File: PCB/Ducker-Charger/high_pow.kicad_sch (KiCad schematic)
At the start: 75 parts, among them Q13 BSC040N08NS5, Q15 SI7157DP-T1-GE3, Q3 BSC040N08NS5, Q4 BSC040N08NS5, Q5 BSC040N08NS5, U1 BQ25713RSNR, U2 TPS25750DRJKR

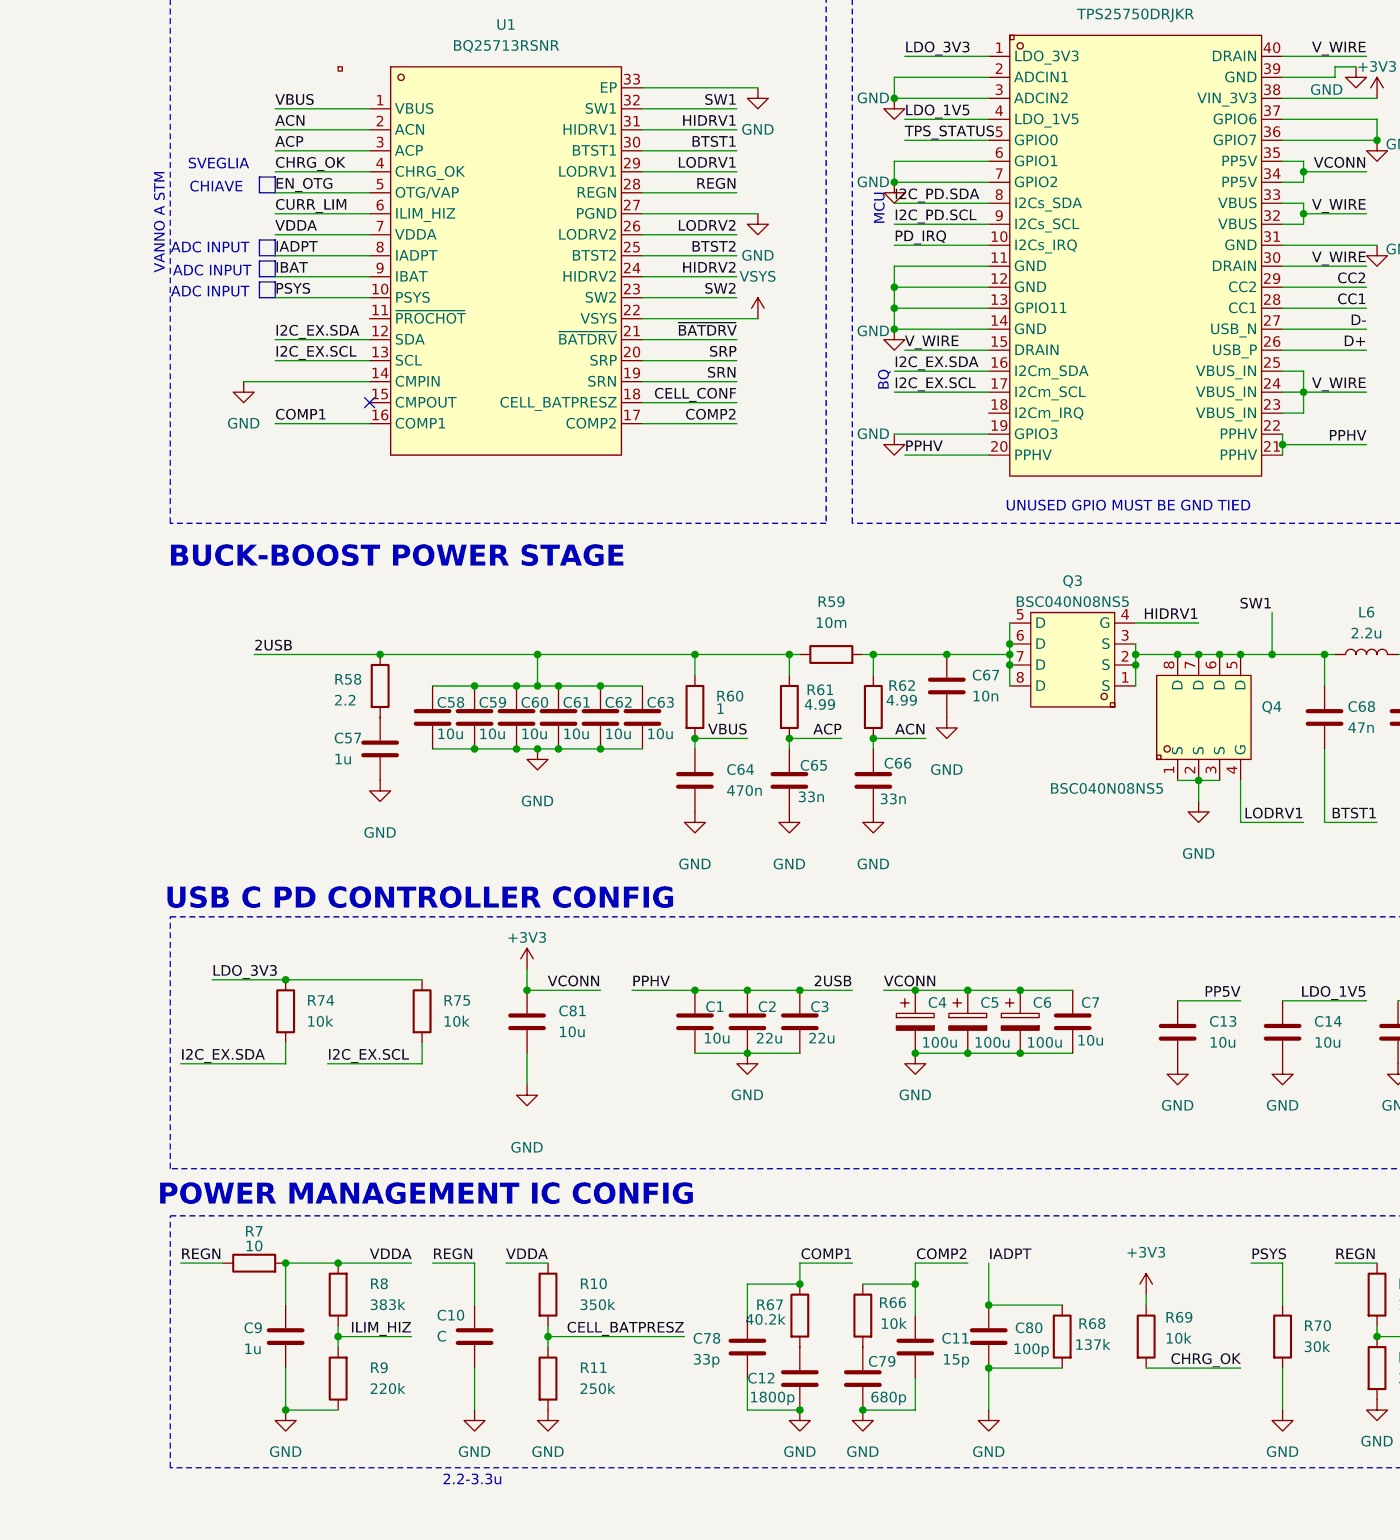
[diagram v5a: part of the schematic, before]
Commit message: fix: MCU connections
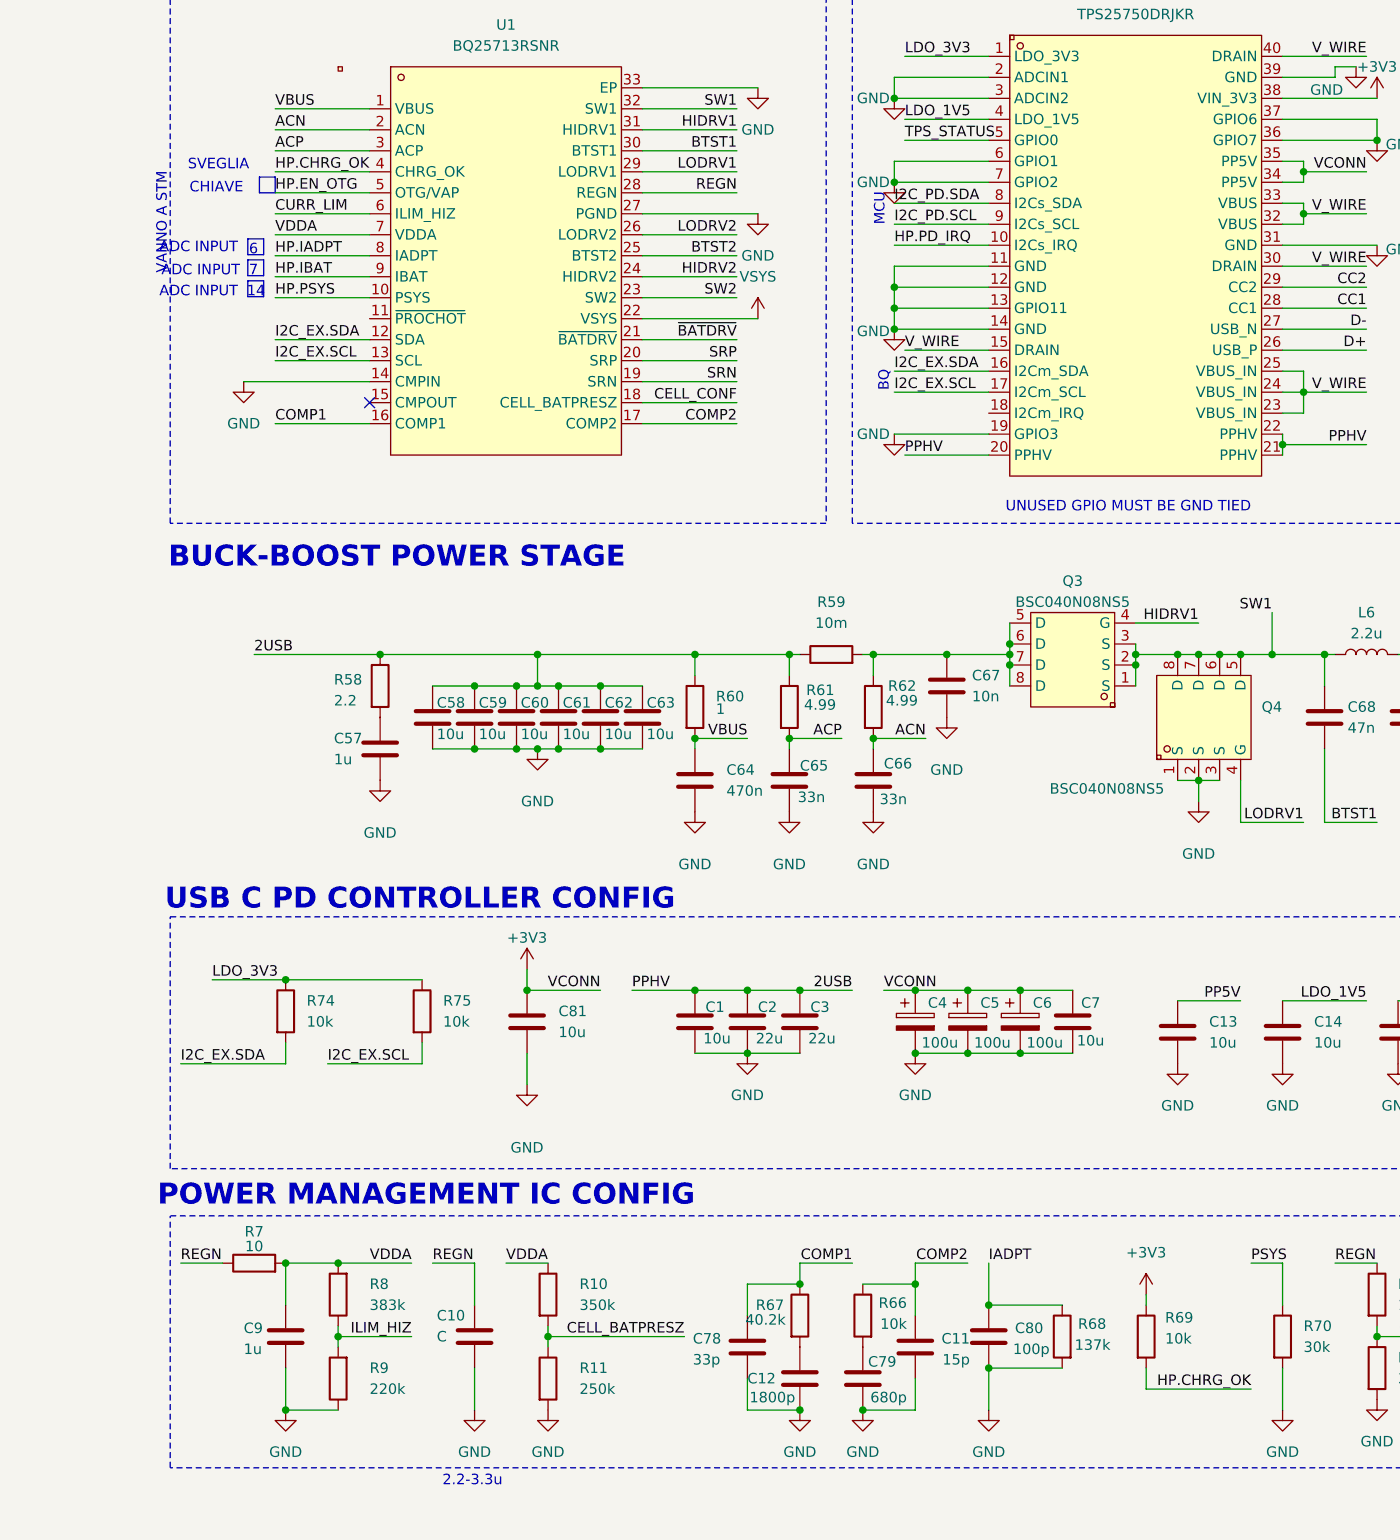
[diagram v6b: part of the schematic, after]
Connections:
- net CHRG_OK is gone; now on net HP.CHRG_OK: R69.2, U1.4 (CHRG_OK)
- net EN_OTG is gone; now on net HP.EN_OTG: U1.5 (OTG/VAP)
- net IBAT is gone; now on net HP.IBAT: U1.9 (IBAT)
- net PD_IRQ is gone; now on net HP.PD_IRQ: U2.10 (I2Cs_IRQ)
- net HP.IADPT: now also U1.8 (IADPT)
- net HP.PSYS: now also U1.10 (PSYS)
- net IADPT: no longer U1.8 (IADPT)
- net PSYS: no longer U1.10 (PSYS)
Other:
- note added: "14"
- note added: "6"
- note added: "7"
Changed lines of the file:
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@@
 	)
 	(rectangle
-		(start 24.765 53.975)
-		(end 26.67 55.88)
+		(start 23.368 53.848)
+		(end 25.273 55.753)
 		(stroke
 			(width 0)
@@
 	)
 	(rectangle
-		(start 24.765 48.895)
-		(end 26.67 50.8)
+		(start 23.368 48.768)
+		(end 25.273 50.673)
 		(stroke
 			(width 0)
@@
 	)
 	(rectangle
-		(start 24.765 51.435)
-		(end 26.67 53.34)
+		(start 23.368 51.308)
+		(end 25.273 53.213)
 		(stroke
 			(width 0)
@@
 		)
 	)
+	(text "6"
+		(exclude_from_sim no)
+		(at 23.495 50.165 0)
+		(effects
+			(font
+				(size 1.27 1.27)
+			)
+			(justify left)
+		)
+	)
 	(text "SVEGLIA"
 		(exclude_from_sim no)
@@
 		)
 	)
+	(text "14"
+		(exclude_from_sim no)
+		(at 23.241 55.245 0)
+		(effects
+			(font
+				(size 1.27 1.27)
+			)
+			(justify left)
+		)
+	)
 	(text "PD_IRQ must be connected to an INTERRUPT on the STM\n"
 		(exclude_from_sim no)
@@
 	(text "ADC INPUT"
 		(exclude_from_sim no)
-		(at 18.796 50.038 0)
+		(at 17.399 49.911 0)
 		(effects
 			(font
@@
 	(text "ADC INPUT"
 		(exclude_from_sim no)
-		(at 19.05 52.832 0)
+		(at 17.653 52.705 0)
 		(effects
 			(font
@@
 		)
 	)
+	(text "7"
+		(exclude_from_sim no)
+		(at 23.495 52.705 0)
+		(effects
+			(font
+				(size 1.27 1.27)
+			)
+			(justify left)
+		)
+	)
 	(text "VANNO A STM"
 		(exclude_from_sim no)
-		(at 12.7 53.086 90)
+		(at 12.954 53.086 90)
 		(effects
 			(font
@@
 	(text "ADC INPUT"
 		(exclude_from_sim no)
-		(at 18.796 55.372 0)
+		(at 17.399 55.245 0)
 		(effects
 			(font
@@
 	(wire
 		(pts
-			(xy 143.51 185.42) (xy 132.08 185.42)
-		)
-		(stroke
-			(width 0)
-			(type default)
-		)
-	)
-	(wire
-		(pts
 			(xy 57.15 139.7) (xy 57.15 137.16)
 		)
@@
 	(wire
 		(pts
+			(xy 132.08 187.96) (xy 144.78 187.96)
+		)
+		(stroke
+			(width 0)
+			(type default)
+		)
+	)
+	(wire
+		(pts
 			(xy 241.3 115.57) (xy 241.3 118.11)
 		)
@@
 	(wire
 		(pts
+			(xy 132.08 187.96) (xy 132.08 185.42)
+		)
+		(stroke
+			(width 0)
+			(type default)
+		)
+	)
+	(wire
+		(pts
 			(xy 116.84 139.7) (xy 123.19 139.7)
 		)
@@
 		)
 	)
+	(label "HP.CHRG_OK"
+		(at 26.67 40.64 0)
+		(effects
+			(font
+				(size 1.27 1.27)
+			)
+			(justify left bottom)
+		)
+	)
 	(label "SYS"
 		(at 209.55 99.06 180)
@@
 		)
 	)
-	(label "PSYS"
-		(at 26.67 55.88 0)
-		(effects
-			(font
-				(size 1.27 1.27)
-			)
-			(justify left bottom)
-		)
-	)
 	(label "CC2"
 		(at 196.85 140.97 180)
@@
 		)
 	)
+	(label "HP.IADPT"
+		(at 26.67 50.8 0)
+		(effects
+			(font
+				(size 1.27 1.27)
+			)
+			(justify left bottom)
+		)
+	)
 	(label "VBUS"
 		(at 26.67 33.02 0)
@@
 		)
 	)
-	(label "IBAT"
-		(at 26.67 53.34 0)
-		(effects
-			(font
-				(size 1.27 1.27)
-			)
-			(justify left bottom)
-		)
-	)
 	(label "LODRV2"
 		(at 189.23 119.38 180)
@@
 		)
 	)
-	(label "EN_OTG"
-		(at 26.67 43.18 0)
+	(label "HP.PSYS"
+		(at 26.67 55.88 0)
 		(effects
 			(font
@@
 		)
 	)
-	(label "PD_IRQ"
-		(at 101.6 49.53 0)
-		(effects
-			(font
-				(size 1.27 1.27)
-			)
-			(justify left bottom)
-		)
-	)
 	(label "BTST1"
 		(at 160.02 119.38 180)
@@
 		)
 	)
+	(label "HP.EN_OTG"
+		(at 26.67 43.18 0)
+		(effects
+			(font
+				(size 1.27 1.27)
+			)
+			(justify left bottom)
+		)
+	)
 	(label "I2C_EX.SDA"
 		(at 15.24 148.59 0)
@@
 		)
 	)
+	(label "HP.IBAT"
+		(at 26.67 53.34 0)
+		(effects
+			(font
+				(size 1.27 1.27)
+			)
+			(justify left bottom)
+		)
+	)
 	(label "ILIM_HIZ"
 		(at 43.18 181.61 180)
@@
 		)
 	)
-	(label "CHRG_OK"
-		(at 143.51 185.42 180)
+	(label "HP.CHRG_OK"
+		(at 144.78 187.96 180)
 		(effects
 			(font
@@
 		)
 	)
-	(label "CHRG_OK"
-		(at 26.67 40.64 0)
-		(effects
-			(font
-				(size 1.27 1.27)
-			)
-			(justify left bottom)
-		)
-	)
 	(label "COMP1"
 		(at 26.67 71.12 0)
@@
 		)
 	)
-	(label "IADPT"
-		(at 26.67 50.8 0)
-		(effects
-			(font
-				(size 1.27 1.27)
-			)
-			(justify left bottom)
-		)
-	)
 	(label "ACP"
 		(at 95.25 109.22 180)
@@
 		)
 	)
+	(label "HP.PD_IRQ"
+		(at 101.6 49.53 0)
+		(effects
+			(font
+				(size 1.27 1.27)
+			)
+			(justify left bottom)
+		)
+	)

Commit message: feat: remade the PCB & minor schematic fixes
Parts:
- removed C13: 10u, Capacitor_SMD:C_0805_2012Metric, symbol Device:C
- removed C66: 33n, symbol Device:C
- removed Q15: SI7157DP-T1-GE3, EasyEDA:POWERPAK-SO-8_L5.9-W4.9-P1.27-LS6.2-BL, symbol EasyEDA:SI7157DP-T1-GE3
- removed R71: 100k, Resistor_SMD:R_0603_1608Metric, symbol Device:R
- removed R72: 300k, Resistor_SMD:R_0603_1608Metric, symbol Device:R
- added C219: 4.7u, Capacitor_SMD:C_0805_2012Metric, symbol Device:C
- added C227: 100p, Capacitor_SMD:C_0603_1608Metric, symbol Device:C
- added C232: 10u 25V, Capacitor_SMD:C_1206_3216Metric, symbol Device:C
- added C242, C246: 100n, Capacitor_SMD:C_0603_1608Metric, symbol Device:C
- added C244, C245: 22u 16V, Capacitor_SMD:C_0805_2012Metric, symbol Device:C
- added L202: 10u 5A, Inductor_SMD:L_7.3x7.3_H4.5, symbol Device:L
- added Q205: AO4407A, EasyEDA:SOIC-8_L4.9-W3.9-P1.27-LS6.0-BL, symbol EasyEDA:AO4407A
- added R218: 150k, Resistor_SMD:R_0603_1608Metric, symbol Device:R
- added R219: 27k, Resistor_SMD:R_0603_1608Metric, symbol Device:R
- added R224: 100k, Resistor_SMD:R_0603_1608Metric, symbol Device:R
- added R225: 13.3k, Resistor_SMD:R_0603_1608Metric, symbol Device:R
- added U203: TPS54302, Package_TO_SOT_SMD:SOT-23-6, symbol Regulator_Switching:TPS54302
- C201: renamed from C9; footprint (none) -> Capacitor_SMD:C_0805_2012Metric
- C202: renamed from C57; footprint (none) -> Capacitor_SMD:C_0805_2012Metric
- C203: renamed from C58; value 10u -> 10u 35V; footprint Capacitor_SMD:C_0603_1608Metric -> Capacitor_SMD:C_1206_3216Metric
- C204: renamed from C59; value 10u -> 10u 35V; footprint Capacitor_SMD:C_0603_1608Metric -> Capacitor_SMD:C_1206_3216Metric
- C205: renamed from C10; value C -> 3.3u; footprint (none) -> Capacitor_SMD:C_0805_2012Metric
- C206: renamed from C60; value 10u -> 10u 35V; footprint Capacitor_SMD:C_0603_1608Metric -> Capacitor_SMD:C_1206_3216Metric
- C207: renamed from C81; value 10u -> 10u 16V
- C208: renamed from C61; value 10u -> 10u 35V; footprint Capacitor_SMD:C_0603_1608Metric -> Capacitor_SMD:C_1206_3216Metric
- C209: renamed from C62; value 10u -> 10u 35V; footprint Capacitor_SMD:C_0603_1608Metric -> Capacitor_SMD:C_1206_3216Metric
- C210: renamed from C63; value 10u -> 10u 35V; footprint Capacitor_SMD:C_0603_1608Metric -> Capacitor_SMD:C_1206_3216Metric
- C211: renamed from C64; footprint (none) -> Capacitor_SMD:C_0805_2012Metric
- C212: renamed from C1; value 10u -> 10u 35V; footprint (none) -> Capacitor_SMD:C_1206_3216Metric
- C213: renamed from C2; value 22u -> 22u 35V; footprint (none) -> Capacitor_SMD:C_1210_3225Metric
- C214: renamed from C78; footprint (none) -> Capacitor_SMD:C_0603_1608Metric
- C215: renamed from C65; footprint (none) -> Capacitor_SMD:C_0603_1608Metric
- C216: renamed from C3; value 22u -> 22u 35V; footprint (none) -> Capacitor_SMD:C_1210_3225Metric
- C217: renamed from C12; footprint (none) -> Capacitor_SMD:C_0603_1608Metric
- C218: renamed from C79; footprint (none) -> Capacitor_SMD:C_0603_1608Metric
- C220: renamed from C4; value 100u -> 100u 16V; footprint (none) -> Capacitor_SMD:C_1210_3225Metric
- C221: renamed from C11; footprint (none) -> Capacitor_SMD:C_0603_1608Metric
- C223: renamed from C5; value 100u -> 100u 16V; footprint (none) -> Capacitor_SMD:C_1210_3225Metric
- C224: renamed from C80; footprint (none) -> Capacitor_SMD:C_0603_1608Metric
- C225: renamed from C6; value 100u -> 100u 16V; footprint (none) -> Capacitor_SMD:C_1210_3225Metric
- C226: renamed from C7; value 10u -> 10u 16V; footprint (none) -> Capacitor_SMD:C_0603_1608Metric
- C229: renamed from C68; footprint (none) -> Capacitor_SMD:C_0603_1608Metric
- C231: renamed from C69; footprint (none) -> Capacitor_SMD:C_0603_1608Metric
- C233: renamed from C8; footprint (none) -> Capacitor_SMD:C_0603_1608Metric
- C234: renamed from C82; footprint (none) -> Capacitor_SMD:C_0603_1608Metric
- C235: renamed from C70; value 10u -> 10u 25V; footprint Capacitor_SMD:C_0603_1608Metric -> Capacitor_SMD:C_1206_3216Metric
- C236: renamed from C71; value 10u -> 10u 25V; footprint Capacitor_SMD:C_0603_1608Metric -> Capacitor_SMD:C_1206_3216Metric
- C237: renamed from C72; value 10u -> 10u 25V; footprint Capacitor_SMD:C_0603_1608Metric -> Capacitor_SMD:C_1206_3216Metric
- C238: renamed from C73; value 10u -> 10u 25V; footprint Capacitor_SMD:C_0603_1608Metric -> Capacitor_SMD:C_1206_3216Metric
- C239: renamed from C74; value 10u -> 10u 25V; footprint Capacitor_SMD:C_0603_1608Metric -> Capacitor_SMD:C_1206_3216Metric
- C240: renamed from C75; value 10u -> 10u 25V; footprint Capacitor_SMD:C_0603_1608Metric -> Capacitor_SMD:C_1206_3216Metric
- C241: renamed from C77; footprint (none) -> Capacitor_SMD:C_0805_2012Metric
- C243: renamed from C76; footprint (none) -> Capacitor_SMD:C_0805_2012Metric
- L201: renamed from L6; value 2.2u -> 2.2u 20A; footprint Inductor_SMD:L_12x12mm_H6mm -> Inductor_SMD:L_Chilisin_BMRF00131360; prod name (none) -> KOHERelec MDA1350-2R2M
- R201: renamed from R7; footprint (none) -> Resistor_SMD:R_0603_1608Metric
- R205: renamed from R58; footprint (none) -> Resistor_SMD:R_0603_1608Metric
- R207: renamed from R10; value 350k -> 330k
- R208: renamed from R11; value 250k -> 1M
- R209: renamed from R60; footprint (none) -> Resistor_SMD:R_0603_1608Metric
- R210: renamed from R61; footprint (none) -> Resistor_SMD:R_0603_1608Metric
- R214: renamed from R62; footprint (none) -> Resistor_SMD:R_0603_1608Metric
- R220: renamed from R64; footprint (none) -> Resistor_SMD:R_0603_1608Metric
- R222: renamed from R65; footprint (none) -> Resistor_SMD:R_0603_1608Metric
- renumbered C67 to C222, C14 to C228, C15 to C230, D2 to D201, D1 to D202, Q3 to Q201, Q4 to Q202, Q5 to Q203, Q13 to Q204, R74 to R202, R8 to R203, R9 to R204, R75 to R206, R67 to R211, R59 to R212, R66 to R213, R68 to R215, R69 to R216, R70 to R217, R63 to R221, R73 to R223, U1 to U201, U2 to U202, USBC1 to USBC201
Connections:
- net CELL_CONF is gone; now on net CELL_BATPRESZ: U201.18 (CELL_BATPRESZ)
- net CURR_LIM is gone; now on net ILIM_HIZ: U201.6 (ILIM_HIZ)
- net IADPT is gone; now on net HP.IADPT: C224.1, R215.1
- net PSYS is gone; now on net HP.PSYS: R217.1
- net +3V3: now also C246.1; no longer C207.1, C220.1, C223.1, C225.1, C226.1, U202.34 (PP5V), U202.35 (PP5V)
- net ACN: now also C215.2
- net GND: now also U202.18 (I2Cm_IRQ), C219.2, C227.2, C232.2, C244.2, C245.2, C246.2, R219.1, R225.2, U203.1 (GND); no longer C215.2
- net HP.IBAT: now also C227.1
- net VSYS: now also C232.1, Q205.1 (S), Q205.2 (S), Q205.3 (S), R218.1, U203.3 (VIN)
- net V_WIRE: now also C219.1; no longer U202.15 (DRAIN), U202.30 (DRAIN), U202.40 (DRAIN)
- net ~{BATDRV}: now also Q205.4 (G)
- net at C241.1, C243.2, R220.1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: now also Q205.5 (D), Q205.6 (D), Q205.7 (D), Q205.8 (D)
- new net: R218.2, R219.2, U203.5 (EN)
- new net: C242.2, L202.1, U203.2 (SW)
- new net: C242.1, U203.6 (BOOT)
- new net +5V: C207.1, C220.1, C223.1, C225.1, C226.1, C244.1, C245.1, L202.2, R224.1, U202.34 (PP5V), U202.35 (PP5V)
- new net 5V_FB: R224.2, R225.1, U203.4 (FB)
- no-connect marks 3 -> 7
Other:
- note added: "5V Supply"
- moved on the sheet: C207, C212, C213, C215, C216, C220, C223, C225, C226, C228, C230, C233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

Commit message: feat: final version before prod
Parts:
- added C247, C248: 4.7u, Capacitor_SMD:C_0805_2012Metric, symbol Device:C
- added C249: 10n, Capacitor_SMD:C_0603_1608Metric, symbol Device:C
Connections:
- net GND: now also C247.1, C248.2, C249.2
- net VSYS: now also C248.1, C249.1
- net at C222.1, Q201.5 (D), Q201.6 (D)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: now also C247.2
